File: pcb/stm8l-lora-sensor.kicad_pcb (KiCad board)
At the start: 2 copper layers, 33 x 57 mm, 48 parts, among them J1 Conn_01x06, J2 Conn_01x02, J3 Conn_01x04, J4 Conn_01x03, J5 Conn_01x02, J6 Conn_01x02, U1 74HC595, U2 STM8L051F3P, U3 74HC595, U4 CA56-12EWA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

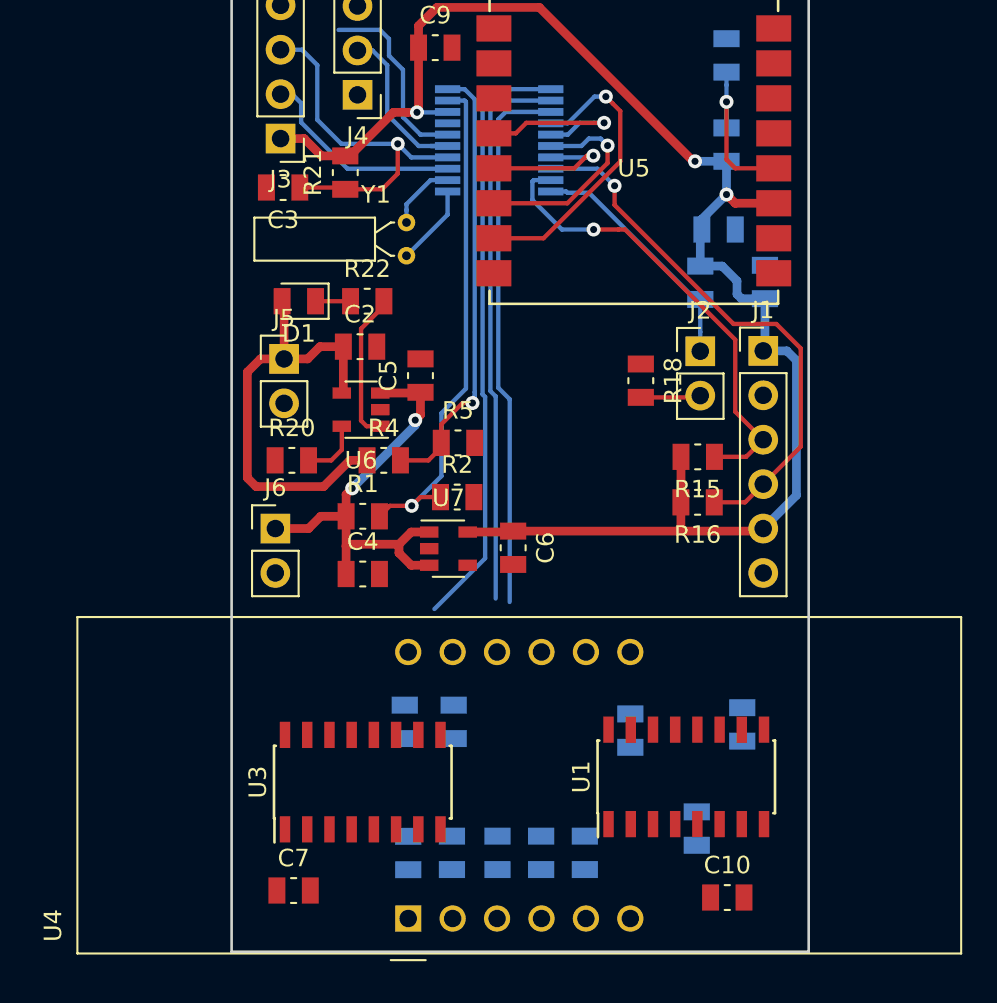
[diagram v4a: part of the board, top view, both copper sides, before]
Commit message: LED IND replaced, pcb almost ready
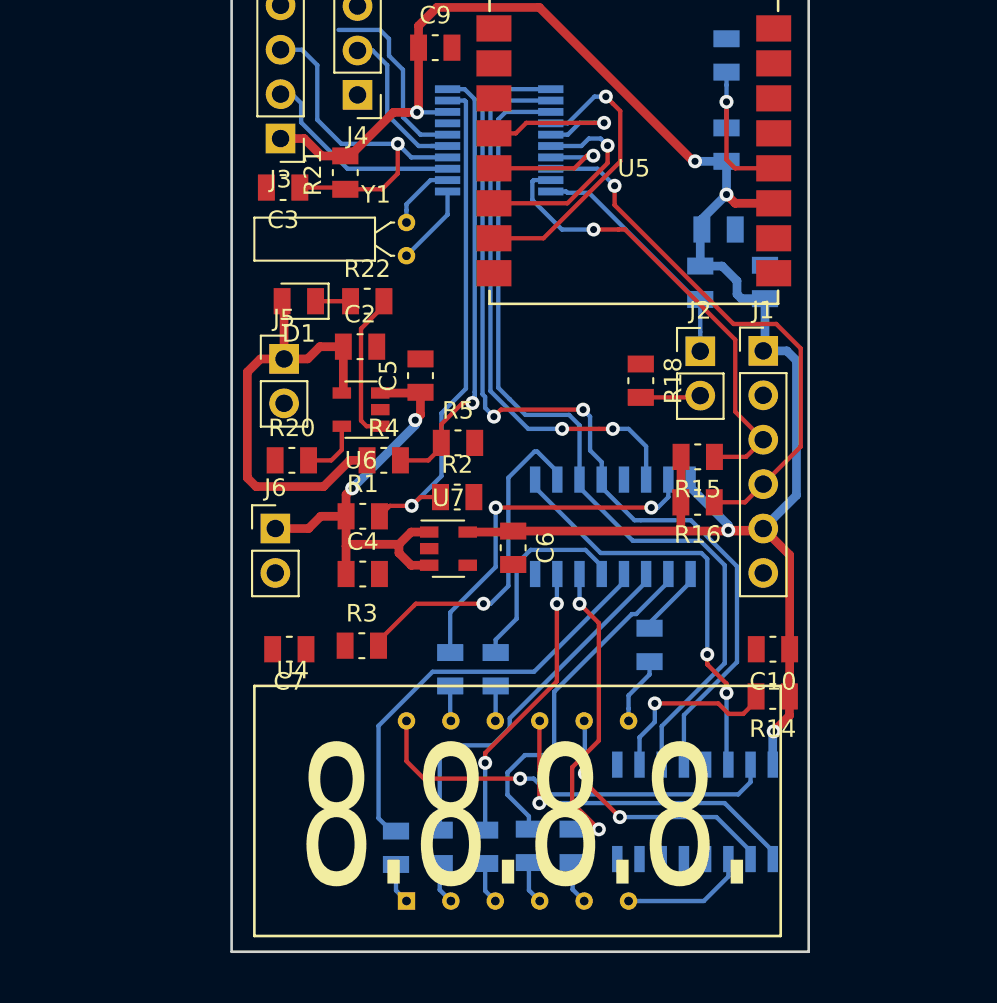
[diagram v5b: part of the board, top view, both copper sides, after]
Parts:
- R14, R3: moved to F.Cu
- U1, U3: moved to B.Cu
- U4: value CA56-12EWA -> HX3641BH; footprint Display_7Segment:CA56-12EWA -> display-led:HX3641BH
- moved R3 22.2 mm to (37.4, 109.5), turned to 0 degrees
- moved R14 21.1 mm to (60.9, 112.4), turned to 180 degrees
- moved U3 19.1 mm to (56.5, 119.0)
- moved U1 14.9 mm to (51.8, 102.7)
- moved R11 14.7 mm to (45.1, 110.8), turned to 270 degrees
- moved C10 14.4 mm to (61.0, 109.7), turned to 180 degrees
- moved C7 13.8 mm to (33.3, 109.7), turned to 180 degrees
- moved R7 5.02 mm to (53.9, 109.5), turned to 270 degrees
- moved R6 3.02 mm to (42.5, 110.8), turned to 270 degrees
- moved U4 1.00 mm to (40.0, 124.1), turned to 0 degrees
- moved R12 0.81 mm to (49.5, 120.9)
- moved R8 0.81 mm to (47.0, 120.9)
- moved R13 0.78 mm to (44.5, 121.0)
- moved R9 0.78 mm to (41.9, 121.0)
- moved R10 0.76 mm to (39.4, 121.1), turned to 270 degrees
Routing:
- net Net-(R10-Pad1): track 0.00 -> 24.5 mm
- net Net-(U1-Pad9): track 0.00 -> 24.3 mm, vias 0 -> 2
- net Net-(U3-Pad15): track 0.00 -> 24.1 mm, vias 0 -> 1
- net Net-(R9-Pad1): track 0.00 -> 21.7 mm
- net Net-(R6-Pad1): track 0.00 -> 20.5 mm, vias 0 -> 2
- net IND_LATCH: track 34.7 -> 55.1 mm, vias 0 -> 2
- net VCC: track 89.1 -> 109.5 mm, vias 3 -> 5
- net Net-(R8-Pad1): track 0.00 -> 20.0 mm
- net Net-(U3-Pad1): track 0.00 -> 19.6 mm, vias 0 -> 1
- net IND_CLK: track 31.0 -> 50.7 mm
- net Net-(R3-Pad2): track 0.00 -> 19.5 mm, vias 0 -> 1
- net Net-(R12-Pad1): track 0.00 -> 17.8 mm, vias 0 -> 2
- net Net-(R13-Pad1): track 0.00 -> 16.4 mm, vias 0 -> 2
- net Net-(U3-Pad2): track 0.00 -> 15.1 mm, vias 0 -> 2
- net Net-(R11-Pad1): track 0.00 -> 11.6 mm
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
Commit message: pcb done
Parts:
- moved R14 2.00 mm to (61.0, 110.4)
- moved C10 1.60 mm to (61.0, 108.1)
- moved R5 0.91 mm to (43.7, 98.4)
- moved C4 0.91 mm to (36.6, 105.3), turned to 270 degrees
- moved C7 0.21 mm to (33.2, 109.5)
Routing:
- net GND: track 0.00 -> 69.2 mm, vias 0 -> 98
- net VCC: track 109.5 -> 126.6 mm
- net DRX: track 10.9 -> 16.8 mm
- net Net-(R14-Pad2): track 10.5 -> 12.5 mm
- net SCL: track 26.6 -> 27.7 mm
- net DTX: track 10.0 -> 10.7 mm
- net IND_DATA: track 32.0 -> 32.6 mm
- net SDA: track 31.1 -> 30.5 mm
- added copper zone on B.Cu, net GND
- added copper zone on F.Cu, net GND
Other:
- board text added: "1"

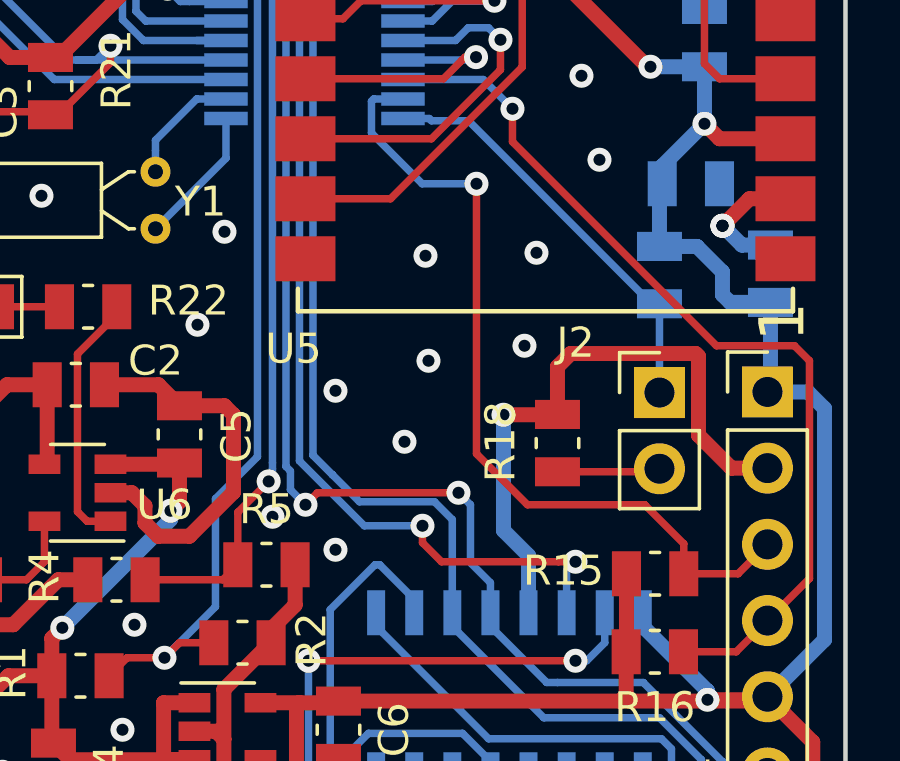
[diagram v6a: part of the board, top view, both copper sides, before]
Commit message: added activity indicator for sensor node
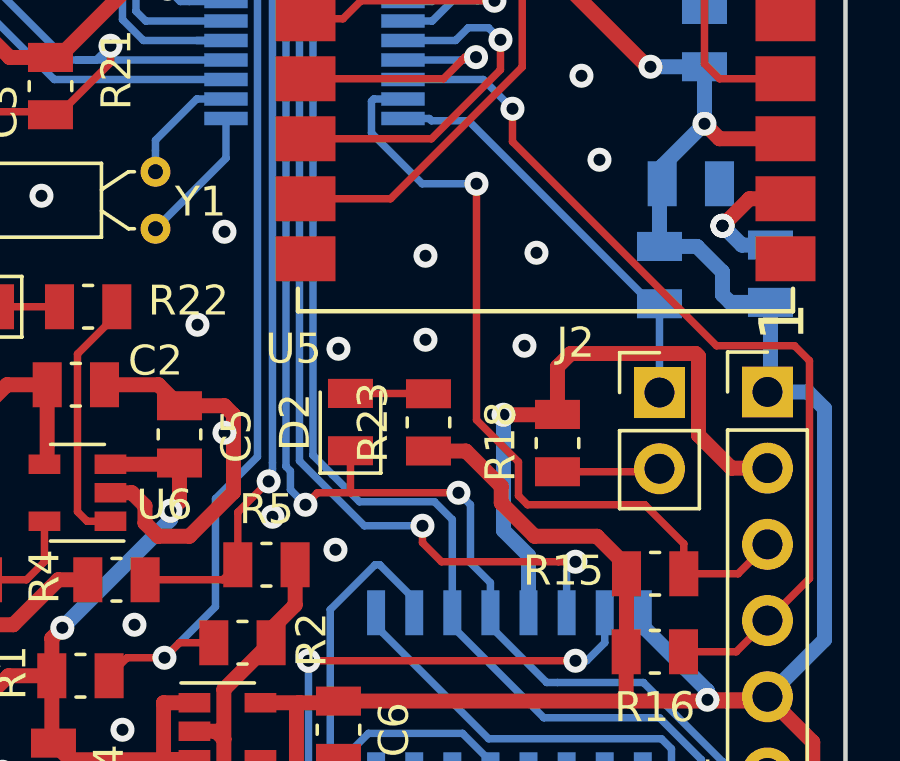
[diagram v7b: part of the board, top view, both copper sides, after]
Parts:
- added D2: LED, LED_SMD:LED_0805_2012Metric, F.Cu at (46.5, 93.6)
- added R23: 1k, Resistor_SMD:R_0805_2012Metric, F.Cu at (49.1, 93.7)
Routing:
- net VCC: track 126.6 -> 135.3 mm
- net Net-(D2-Pad2): track 0.00 -> 2.60 mm
- net IND_LATCH: track 55.1 -> 56.5 mm
